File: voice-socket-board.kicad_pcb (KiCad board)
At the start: 2 copper layers, 150 x 100 mm, 275 parts, among them J1 JACK_MONO_SW, J2 JACK_MONO_SW, J3 JACK_MONO_SW, P1 CONN_01X03, P2 CONN_01X03, P3 CONN_02X05, P4 DDR3-DIMM, Q1 MMBT3904, Q2 DMMT3904W, Q3 2N7002, Q4 2N7002, Q5 MMBT3904, Q6 2N3906, Q7 MMBT3904, Q8 MMBT3904, Q9 MMBT3904, SW1 SPST, SW10 SP3T, SW11 SP3T, SW12 SP3T, SW13 SP3T, SW14 SPST, SW15 TACT_SWITCH, SW2 SPST, SW3 SP3T, SW4 SP3T, SW5 SPST, SW6 SPST, SW7 Switch_SPDT_x2, SW8 2P3T, SW9 SP3T, U1 LM833, U10 TL072-, U11 NE5534, U2 TL072-, U3 TL072-, U4 TL072-, U5 TL072-, U6 TL072-, U7 MAX9945, U8 CD4013, U9 TL072-

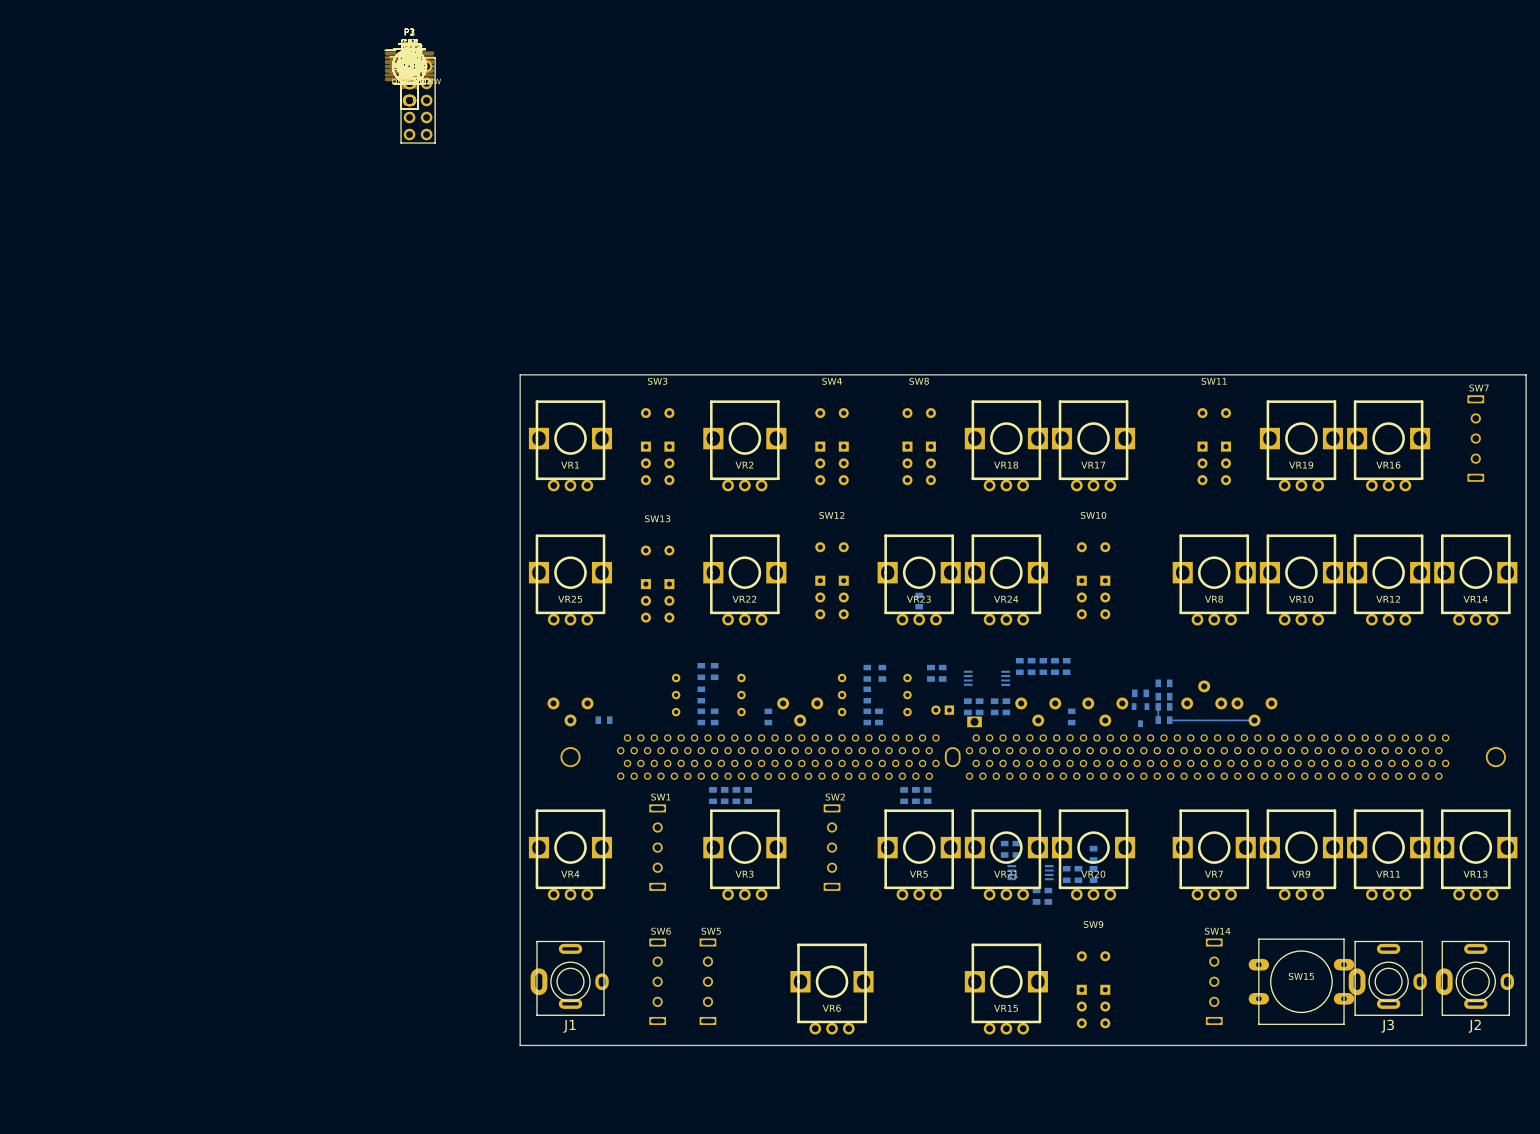
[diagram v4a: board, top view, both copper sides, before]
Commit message: placing components for LFO
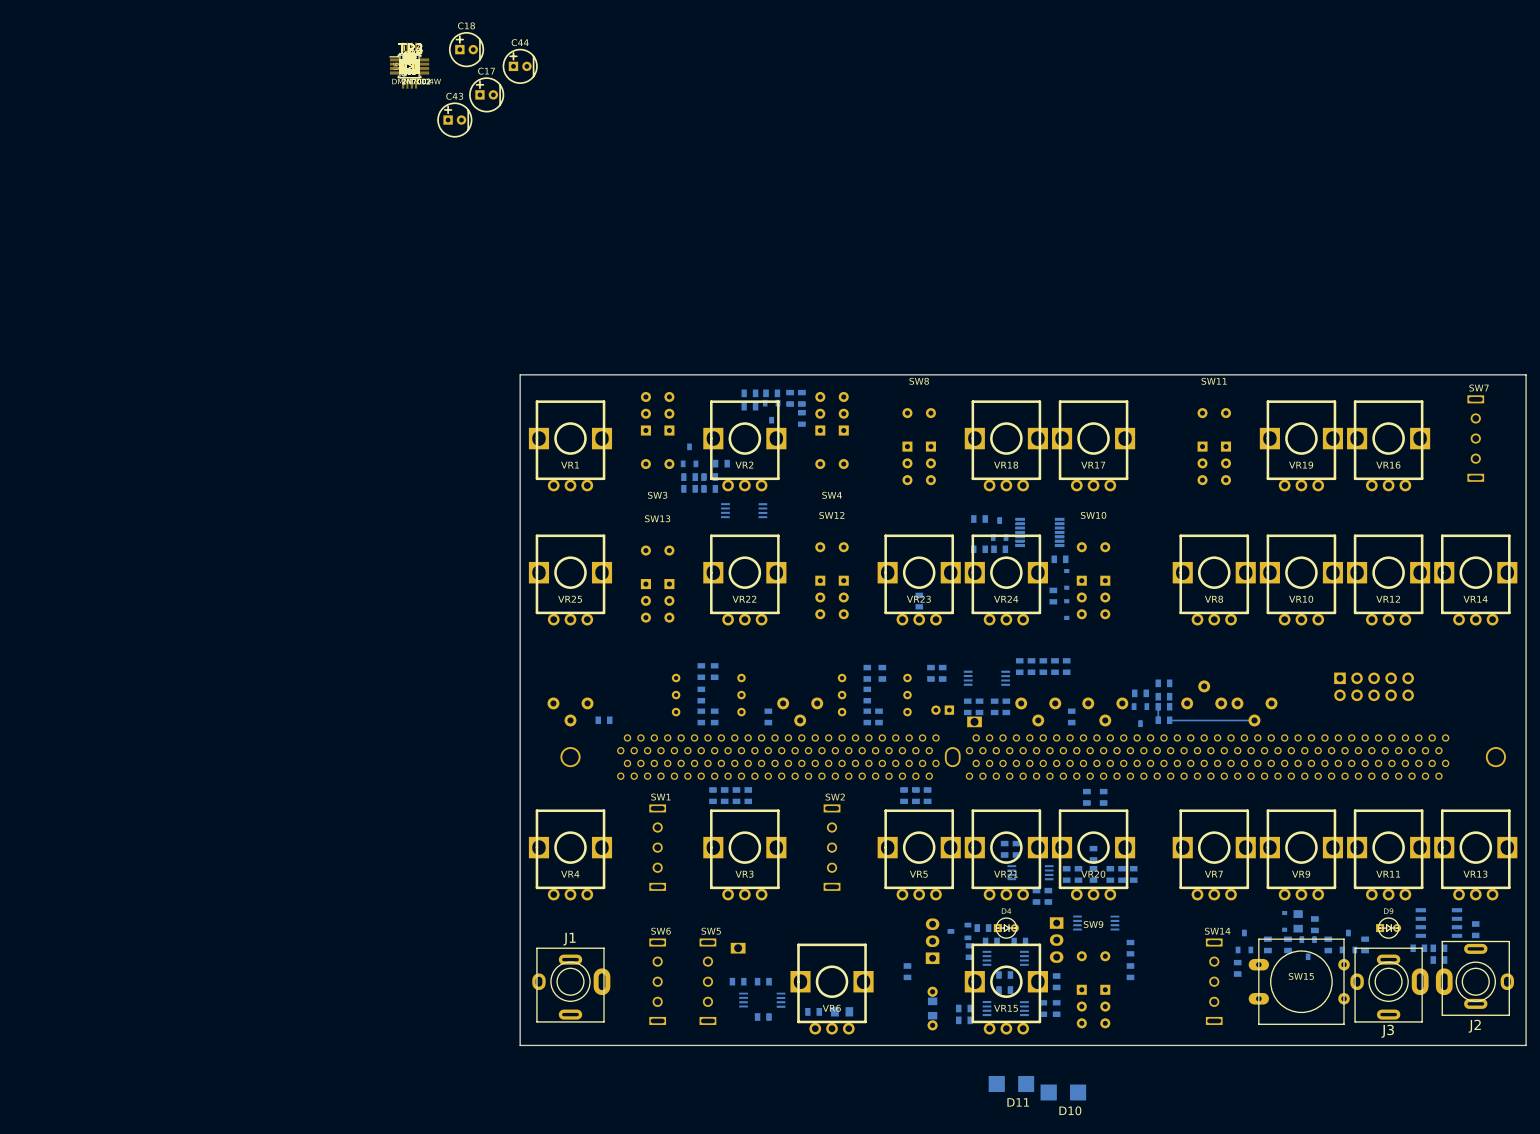
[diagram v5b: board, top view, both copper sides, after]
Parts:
- added C62: 10p, MyModules:SM0603-C-JRL, B.Cu at (182.0, 127.2)
- added D10: D, MyModules:SMB, B.Cu at (126.0, 147.0)
- added D11: D, MyModules:SMB, B.Cu at (118.2, 145.8)
- C14: footprint MyModules:SM0603-C-JRL -> MyModules:CAP-5MM-BOX-0805-COMBO; moved to B.Cu
- C15, C22, C3, C4, C5, C53, C61, D1, D2, D6, D7, D8, P1, P2, P3, Q1, Q5, Q7, Q8, Q9, R114, R115, R116, R117, R118, R120, R121, R122, R123, R19, R20, R21, R22, R23, R24, R25, R26, R27, R28, R29, R30, R31, R48, R49, R50, R51, R52, R53, R54, R55, R58, R60, R61, R62, R64, R77, R79, R80, R81, R82, R83, R87, R88, TP1, U1, U11, U2, U3, U4, U5, U8: moved to B.Cu
- moved R123 204.6 mm to (187.5, 122.8), turned to 90 degrees
- moved R122 202.1 mm to (182.0, 125.5), turned to 180 degrees
- moved R121 199.9 mm to (179.0, 125.5), turned to 180 degrees
- moved U11 199.7 mm to (182.0, 121.8)
- moved D9 194.5 mm to (174.5, 122.5)
- moved R120 193.6 mm to (171.0, 125.0), turned to 90 degrees
- moved Q9 191.4 mm to (168.5, 124.5), turned to 180 degrees
- moved R117 189.5 mm to (165.5, 125.0), turned to 90 degrees
- moved Q8 187.7 mm to (162.5, 125.5)
- moved R115 186.0 mm to (163.5, 122.0), turned to 270 degrees
- moved R118 185.3 mm to (159.5, 125.0), turned to 90 degrees
- moved C61 183.9 mm to (161.0, 121.5), turned to 90 degrees
- moved R116 183.1 mm to (156.5, 125.0), turned to 270 degrees
- moved R114 182.6 mm to (152.0, 128.5), turned to 90 degrees
- moved D8 182.4 mm to (159.0, 121.5), turned to 270 degrees
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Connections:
- U2 pad 1: Net-(R29-Pad2) -> Net-(R31-Pad2)
- U2 pad 2: Net-(R29-Pad2) -> Net-(R31-Pad2)
- U2 pad 3: Net-(J1-Pad3) -> Net-(R30-Pad1)
- U2 pad 5: Net-(R30-Pad1) -> Net-(J1-Pad3)
- U2 pad 6: Net-(R31-Pad2) -> Net-(R29-Pad2)
- U2 pad 7: Net-(R31-Pad2) -> Net-(R29-Pad2)
- U4 pad 1: Net-(D5-Pad1) -> Net-(P2-Pad1)
- U4 pad 2: Net-(R56-Pad1) -> Net-(P2-Pad1)
- U4 pad 3: Net-(D3-Pad2) -> Net-(R60-Pad2)
- U4 pad 5: Net-(R52-Pad2) -> Net-(R54-Pad2)
- U4 pad 6: Net-(P1-Pad1) -> Net-(R62-Pad2)
- U4 pad 7: Net-(P1-Pad1) -> Net-(P2-Pad3)
- U5 pad 1: Net-(P2-Pad1) -> Net-(D5-Pad1)
- U5 pad 2: Net-(P2-Pad1) -> Net-(R56-Pad1)
- U5 pad 3: Net-(R60-Pad2) -> Net-(D3-Pad2)
- U5 pad 5: Net-(R54-Pad2) -> Net-(R52-Pad2)
- U5 pad 6: Net-(R62-Pad2) -> Net-(P1-Pad1)
- U5 pad 7: Net-(P2-Pad3) -> Net-(P1-Pad1)

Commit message: all components but decoupling caps placed. Started routing
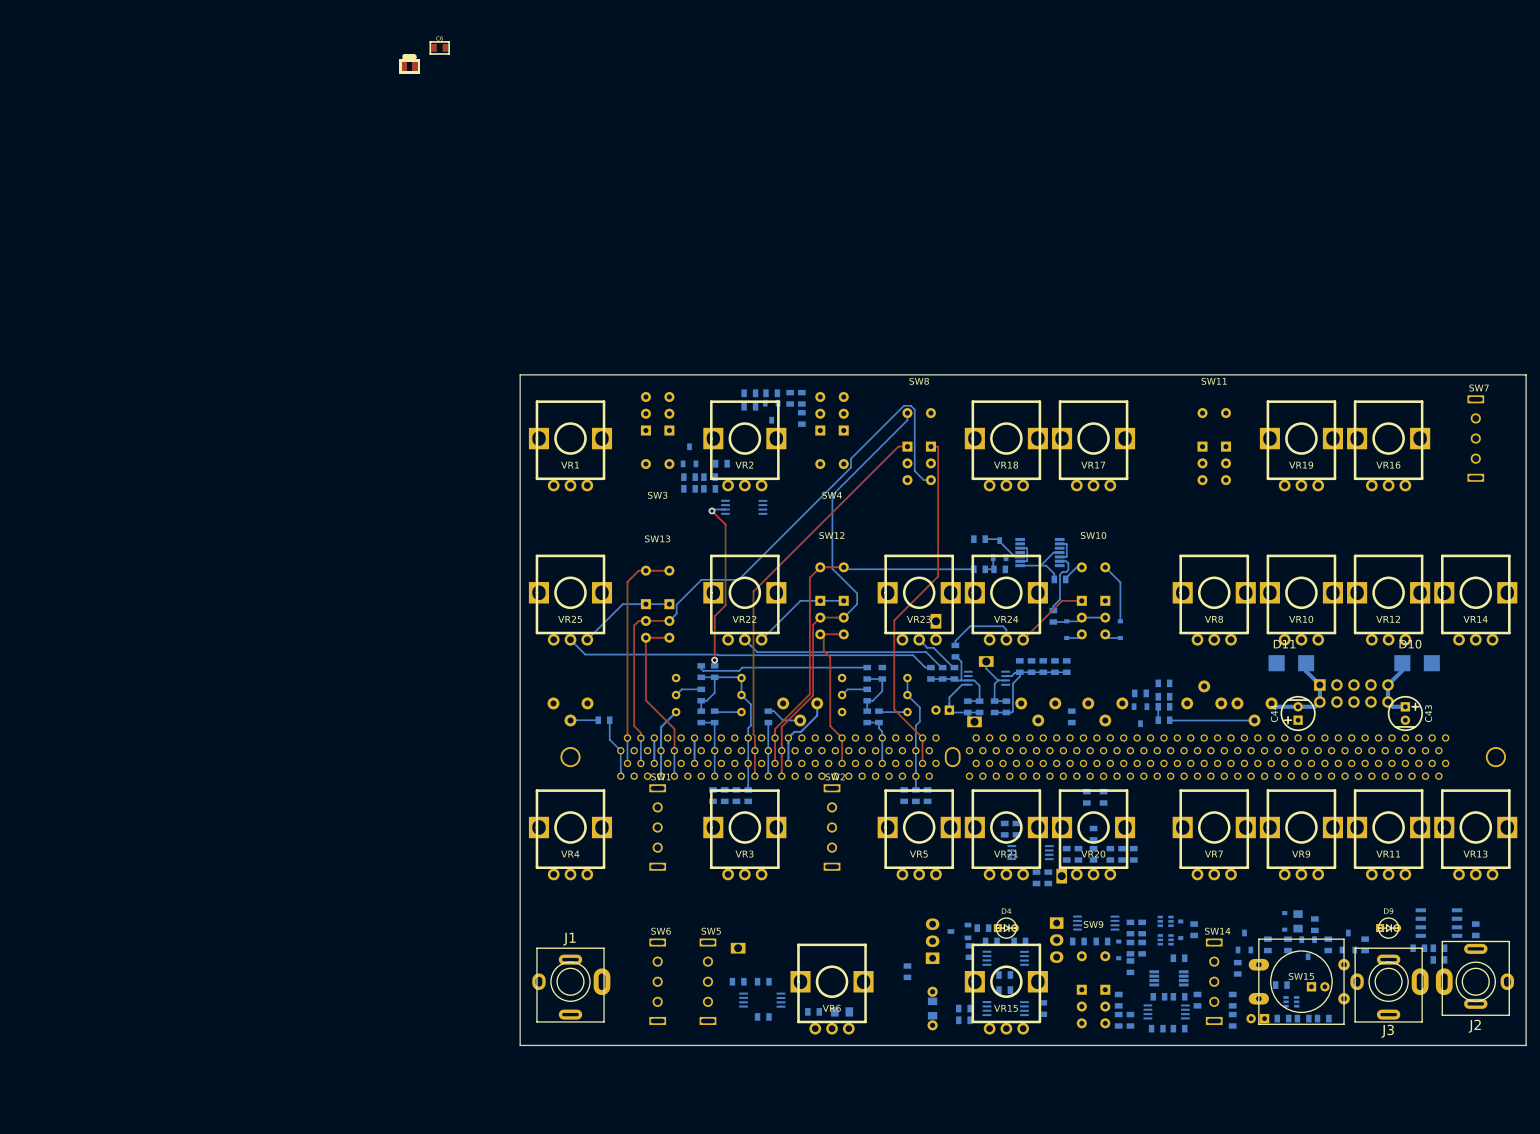
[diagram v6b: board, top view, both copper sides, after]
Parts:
- C16, C17, C18, C19, C20, C21, D3, D5, Q2, Q3, Q4, R112, R56, R57, R59, R63, R65, R66, R67, R68, R69, R70, R72, R73, R74, R75, R76, TP2, TP3, TP4, U6, U7: moved to B.Cu
- moved C16 196.8 mm to (164.8, 136.0), turned to 180 degrees
- moved R63 194.7 mm to (161.8, 136.0), turned to 180 degrees
- moved R65 192.7 mm to (158.8, 136.0)
- moved Q2 191.7 mm to (160.0, 133.5), turned to 90 degrees
- moved R66 188.9 mm to (158.5, 131.0), turned to 180 degrees
- moved R67 187.9 mm to (151.2, 136.2), turned to 270 degrees
- moved C18 186.6 mm to (155.0, 136.0), turned to 180 degrees
- moved C19 185.6 mm to (151.2, 133.2), turned to 90 degrees
- moved R74 183.7 mm to (143.2, 137.5)
- moved R68 182.2 mm to (146.0, 133.2), turned to 270 degrees
- moved C17 181.8 mm to (164.0, 131.2)
- moved R75 181.7 mm to (140.0, 137.5)
- moved U6 180.7 mm to (141.5, 135.0), turned to 270 degrees
- moved R69 180.0 mm to (143.2, 132.8)
- moved R76 178.3 mm to (136.0, 136.2), turned to 90 degrees
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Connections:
- P4 pad 42: Net-(P4-Pad42) -> GND
- SW12 pad 2: VCO2_TRI -> VCO2_PULSE
- SW12 pad 4: VCO2_PULSE -> VCO2_TRI
- SW13 pad 2: VCO1_TRI -> VCO1_PULSE
- SW13 pad 4: VCO1_PULSE -> VCO1_TRI
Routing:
- net VCO1_PULSE: track 0.00 -> 90.3 mm
- net VCO2_PULSE: track 0.00 -> 67.0 mm
- net VCO1_SYNC_IN: track 0.00 -> 59.5 mm
- net Net-(R109-Pad1): track 0.00 -> 55.5 mm
- net VCO2_SAW: track 0.00 -> 55.1 mm
- net VCO2_SYNC_IN: track 0.00 -> 52.7 mm
- net VCO1_PITCH_CV: track 0.00 -> 35.1 mm
- net VCO1_SAW: track 0.00 -> 34.0 mm
- net Net-(R110-Pad1): track 0.00 -> 31.2 mm
- net VCO2_PITCH_CV: track 0.00 -> 29.7 mm
- net +12V: track 0.00 -> 28.4 mm
- net VCO1_OCTAVE: track 0.00 -> 26.7 mm, vias 0 -> 2
- net VCO1_TRI: track 0.00 -> 25.9 mm
- net MASTER_TUNE: track 0.00 -> 25.5 mm
- net -12V: track 0.00 -> 24.8 mm
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
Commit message: routing. 3D viewer is crashing. Trying to remove 3D model associations to see if there are any of my models that are causing the crash
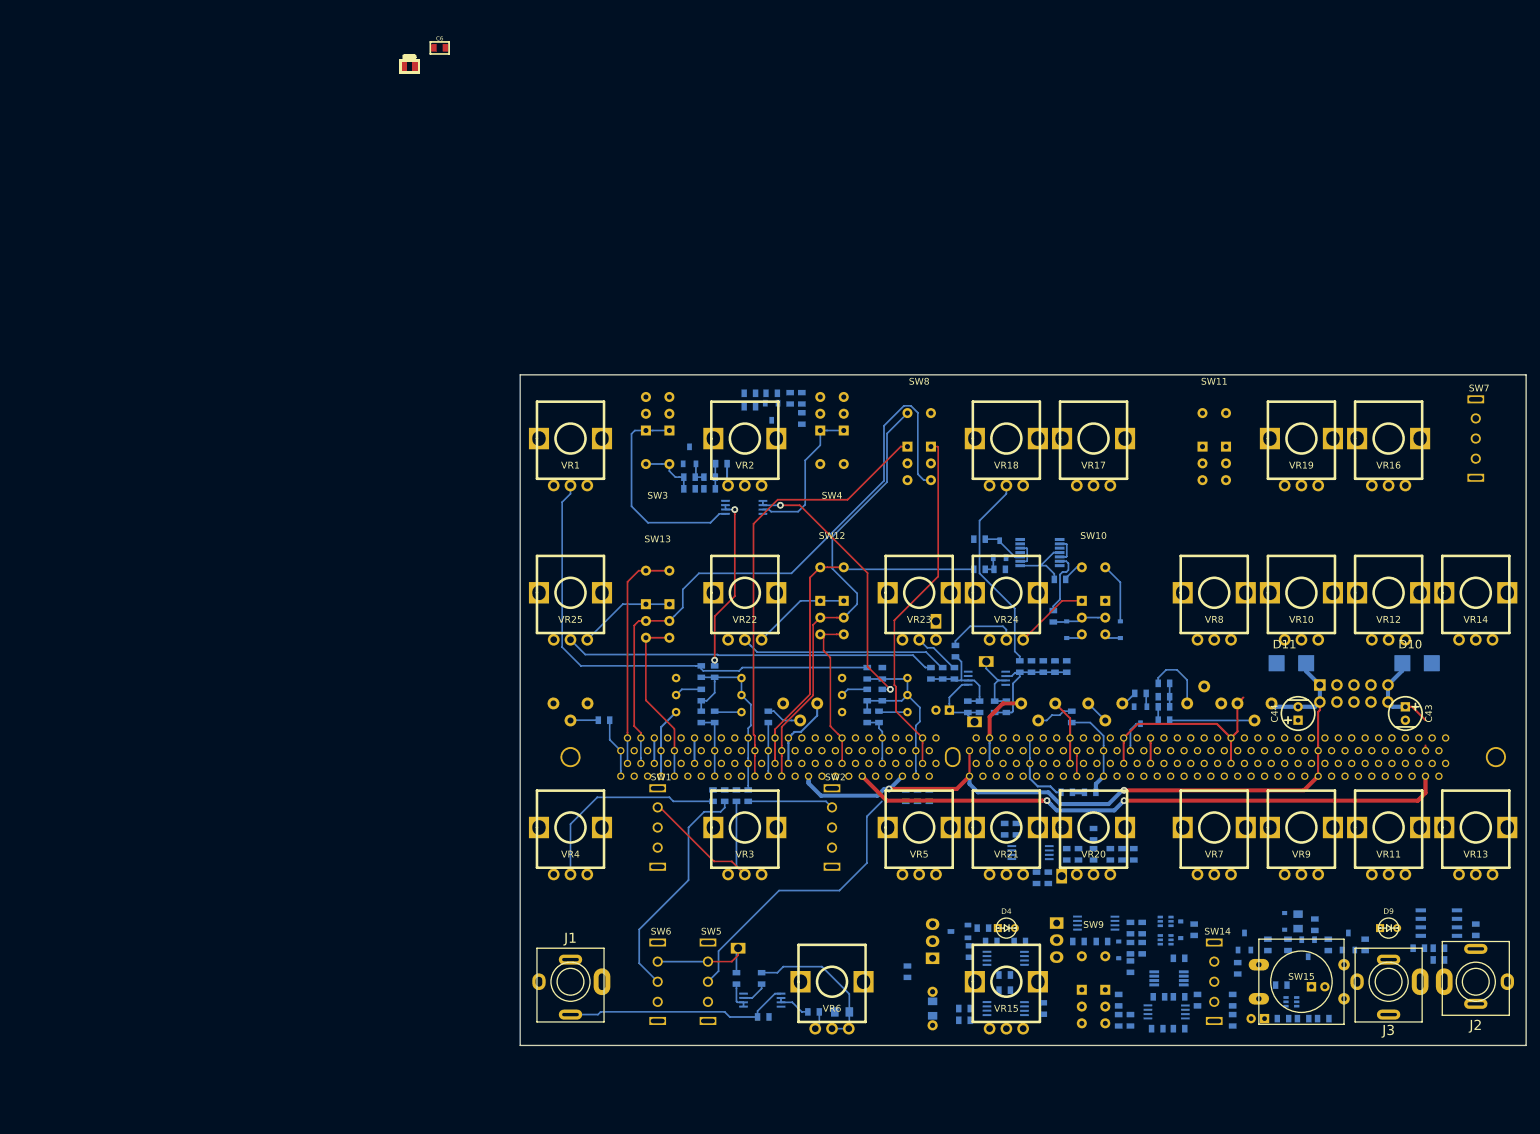
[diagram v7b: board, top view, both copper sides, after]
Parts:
- R12: moved to B.Cu
- moved R12 117.3 mm to (99.0, 87.8), turned to 90 degrees
- moved C22 3.09 mm to (126.5, 102.2), turned to 0 degrees
- moved R77 2.14 mm to (130.0, 102.2), turned to 180 degrees
- moved R14 2.00 mm to (104.2, 102.8)
- moved R4 1.75 mm to (75.5, 102.8)
- moved R6 1.75 mm to (73.8, 102.8)
- moved R10 1.50 mm to (102.5, 102.8)
- moved R30 0.56 mm to (81.0, 130.0), turned to 90 degrees
- moved R31 0.56 mm to (77.2, 130.0), turned to 270 degrees
- moved R11 0.25 mm to (106.0, 102.8)
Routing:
- net +12V: track 28.4 -> 168.1 mm, vias 0 -> 2
- net -12V: track 24.8 -> 142.7 mm, vias 0 -> 2
- net MASTER_TUNE: track 25.5 -> 72.0 mm
- net VCO2_GLIDE_CV: track 0.00 -> 42.9 mm
- net VCO2_OCTAVE: track 0.00 -> 40.4 mm, vias 0 -> 2
- net VCO1_GLIDE_CV: track 0.00 -> 34.8 mm
- net Net-(J1-Pad3): track 0.00 -> 33.8 mm
- net Net-(SW3-Pad3): track 0.00 -> 32.2 mm
- net Net-(R6-Pad2): track 0.00 -> 30.7 mm
- net Net-(R99-Pad2): track 0.00 -> 30.3 mm
- net LFO_MOD: track 0.00 -> 28.6 mm
- net Net-(C5-Pad1): track 0.00 -> 22.8 mm
- net Net-(SW4-Pad3): track 0.00 -> 22.4 mm
- net KEY_TRACK: track 0.00 -> 17.2 mm
- net VCA_IN: track 0.00 -> 14.5 mm
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
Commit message: routing. bit of a nightmare. need to figure out final position of power connector
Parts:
- moved R55 7.85 mm to (110.0, 126.0), turned to 270 degrees
- moved R75 4.00 mm to (144.0, 137.5), turned to 180 degrees
- moved R73 2.66 mm to (136.0, 131.2)
- moved R74 2.00 mm to (141.2, 137.5), turned to 180 degrees
- moved R76 1.82 mm to (136.5, 134.5), turned to 270 degrees
- moved C21 1.77 mm to (134.5, 134.5), turned to 90 degrees
- turned R51 to 0 degrees
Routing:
- net Net-(C14-Pad2): track 0.00 -> 49.6 mm
- net EG1_RELEASE_CV: track 0.00 -> 46.9 mm
- net EG2_SUSTAIN_CV: track 0.00 -> 34.9 mm
- net LFO_PULSE: track 0.00 -> 30.8 mm
- net EG1_SUSTAIN_CV: track 0.00 -> 25.9 mm
- net EG2_RELEASE_CV: track 0.00 -> 20.5 mm
- net EG1_ATTACK_CV: track 0.00 -> 19.5 mm
- net EG1_DECAY_CV: track 0.00 -> 19.1 mm
- net LFO_GATE: track 0.00 -> 17.7 mm
- net Net-(P2-Pad1): track 0.00 -> 17.1 mm, vias 0 -> 1
- net Net-(P2-Pad3): track 0.00 -> 15.1 mm
- net RANDOM: track 0.00 -> 12.2 mm
- net Net-(C14-Pad1): track 0.00 -> 9.97 mm
- net LFO_TRI: track 0.00 -> 8.25 mm
- net Net-(R54-Pad2): track 0.00 -> 8.12 mm
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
